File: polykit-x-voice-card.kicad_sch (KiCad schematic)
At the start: 38 parts, among them J1 Conn_01x36, U1 4016, U2 TL072, U3 4016

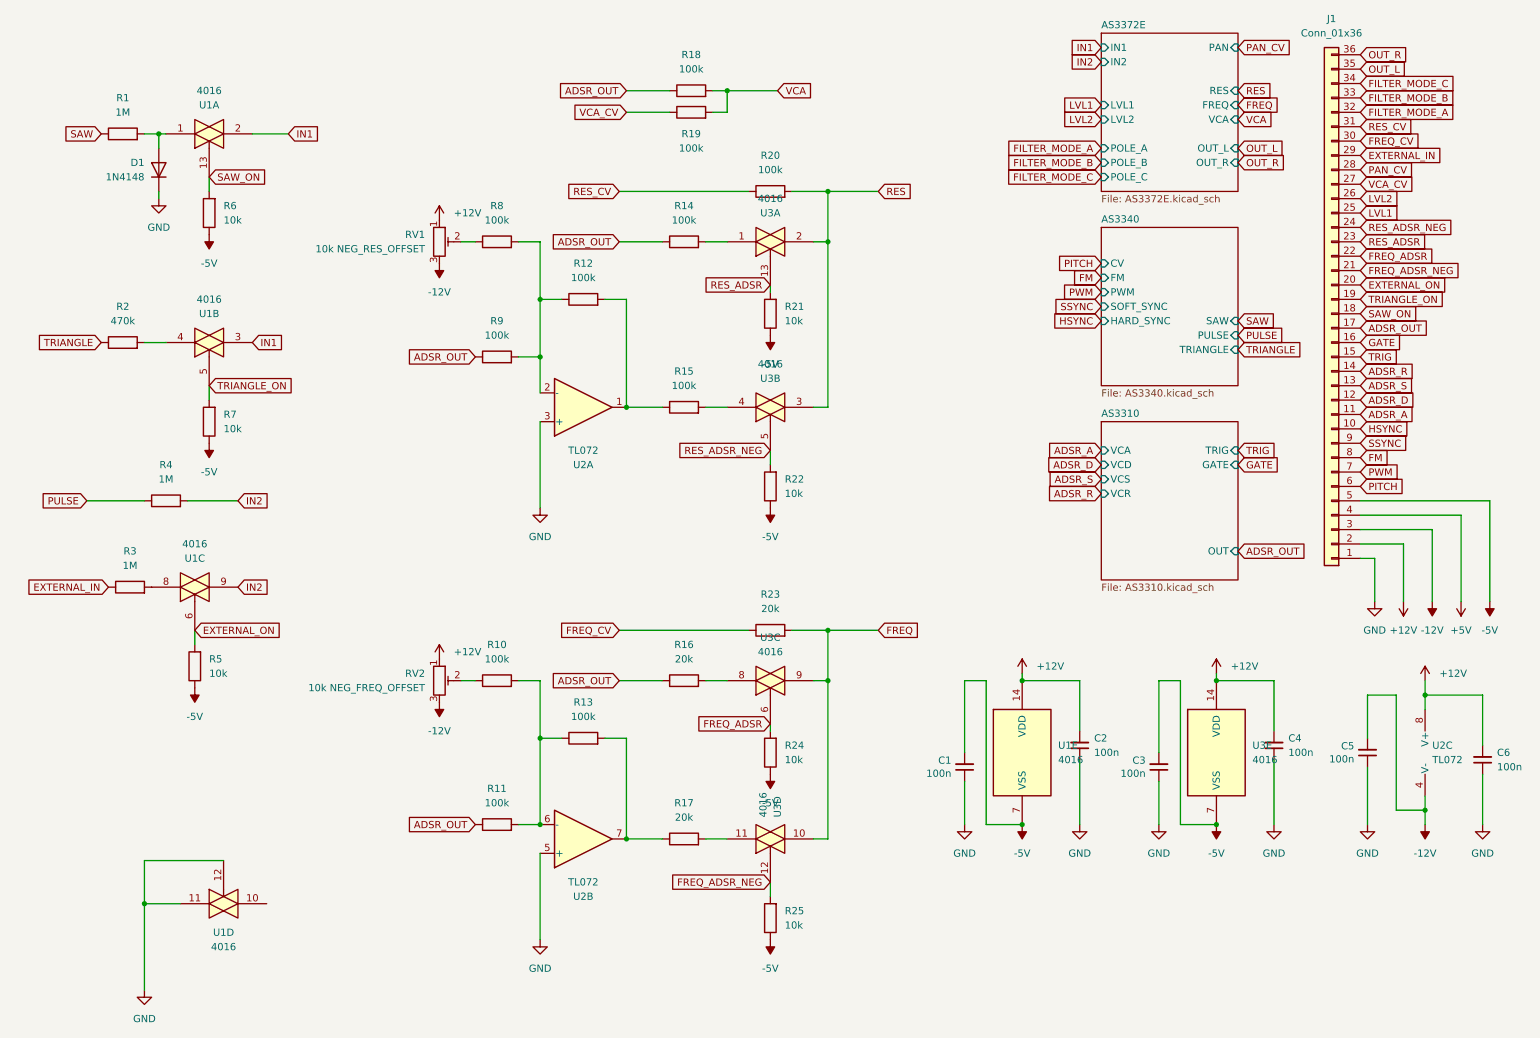
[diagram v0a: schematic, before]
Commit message: - add R38 offset to IN1 - change 4016 to 4066
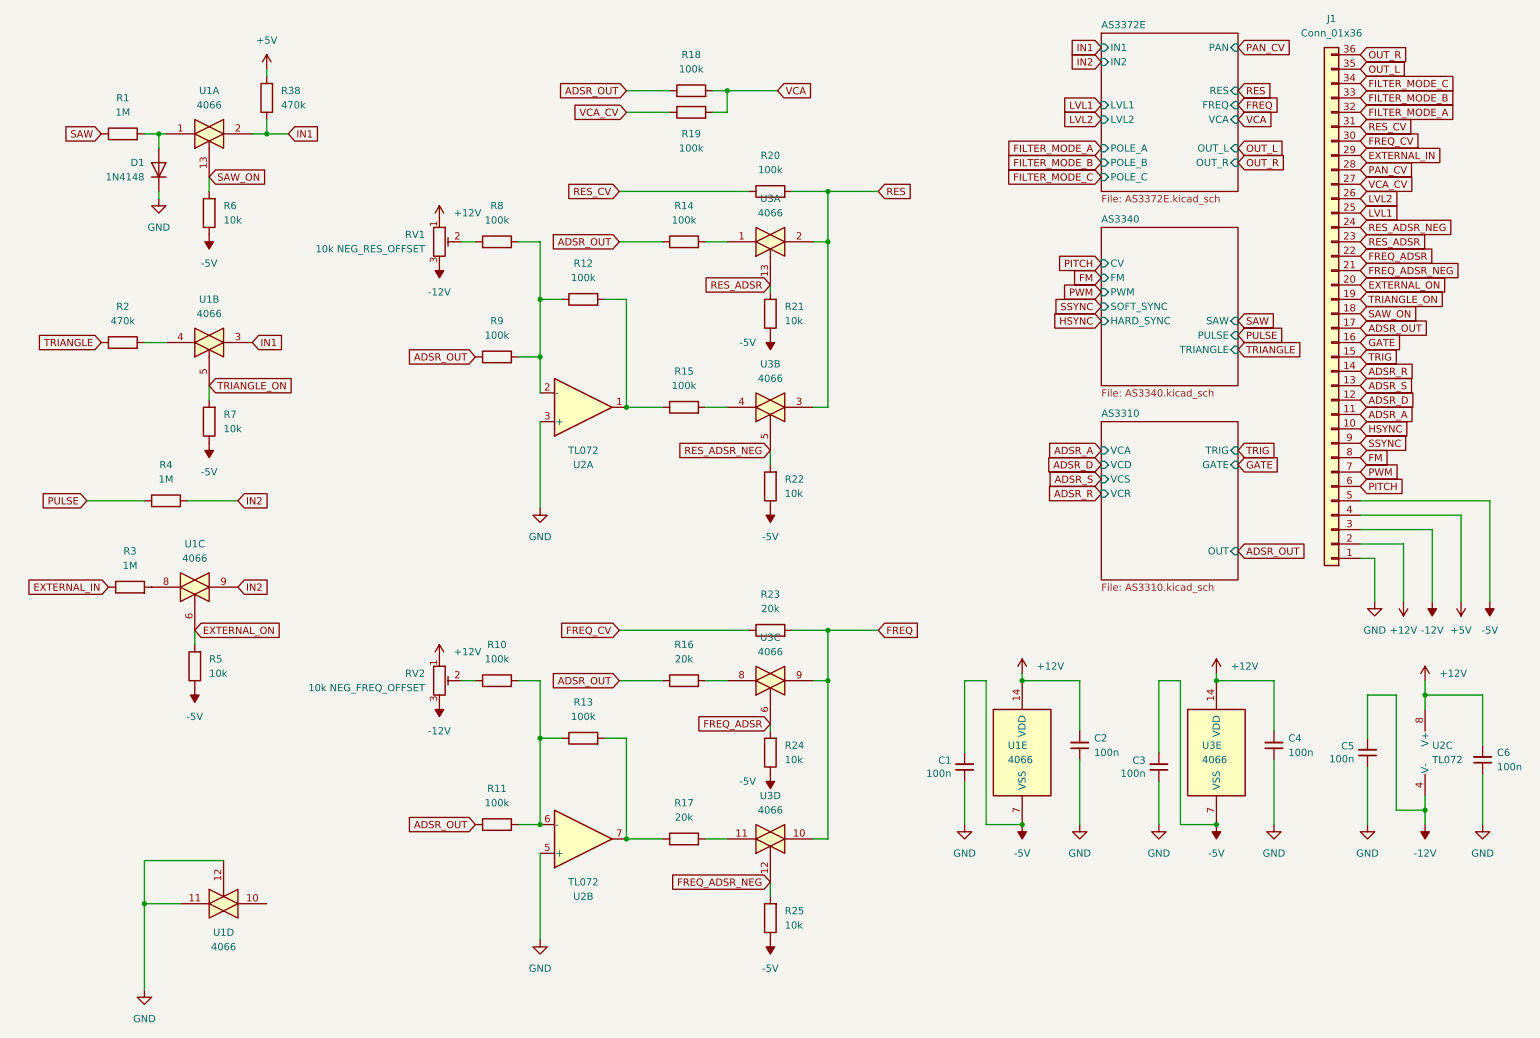
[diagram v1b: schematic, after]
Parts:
- added R38: 470k, Resistor_THT:R_Axial_DIN0207_L6.3mm_D2.5mm_P10.16mm_Horizontal, symbol Device:R
- U1, U3: value 4016 -> 4066; symbol 4xxx:4016 -> 4xxx:4066
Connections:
- net +5V: now also R38.2
- net IN1: now also R38.1
